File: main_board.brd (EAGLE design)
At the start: 100.3 x 74.9 mm, 46 parts, among them P1 ST-TF-003A, U1 STM32F407VGT6, U2 USBLC6-2, U3 MCP1700T-3302E, U4 LTC4054LES5-4.2#TRPBF, X1 MicroUSB-B

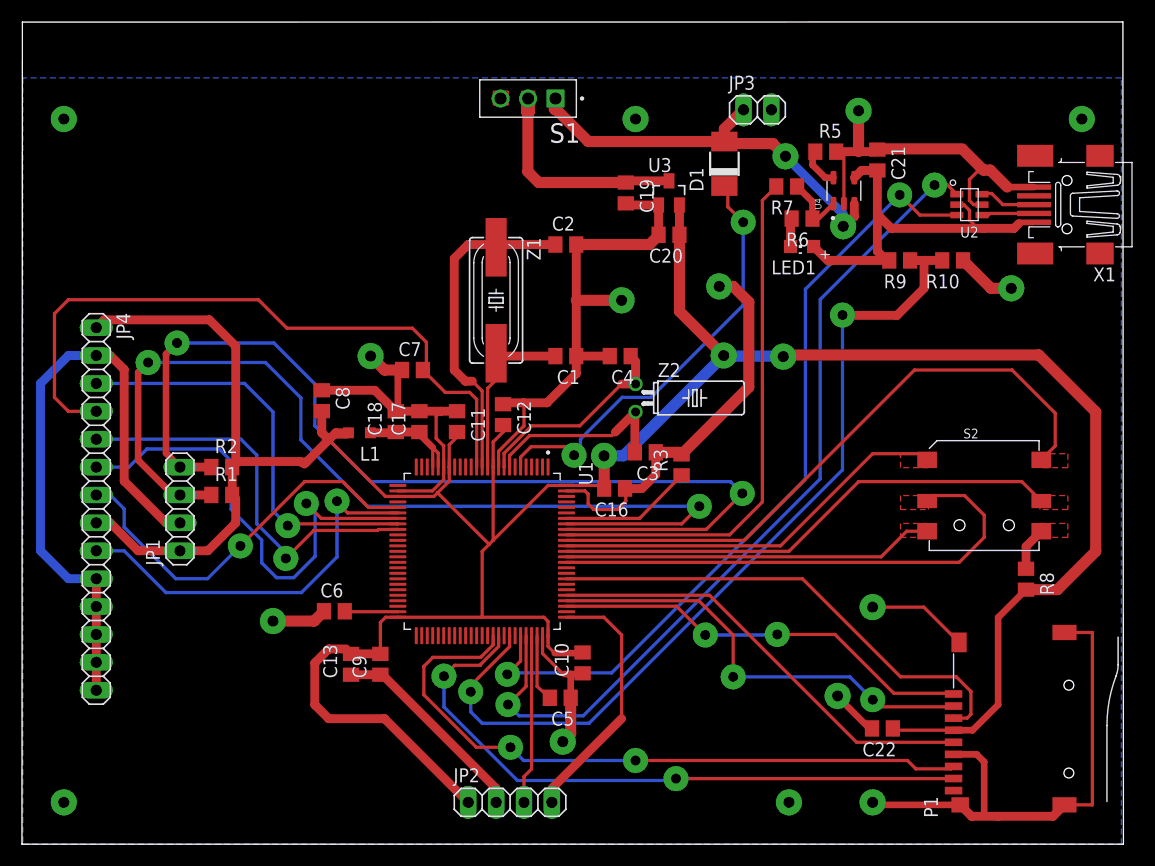
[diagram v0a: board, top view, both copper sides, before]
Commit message: correct board errors
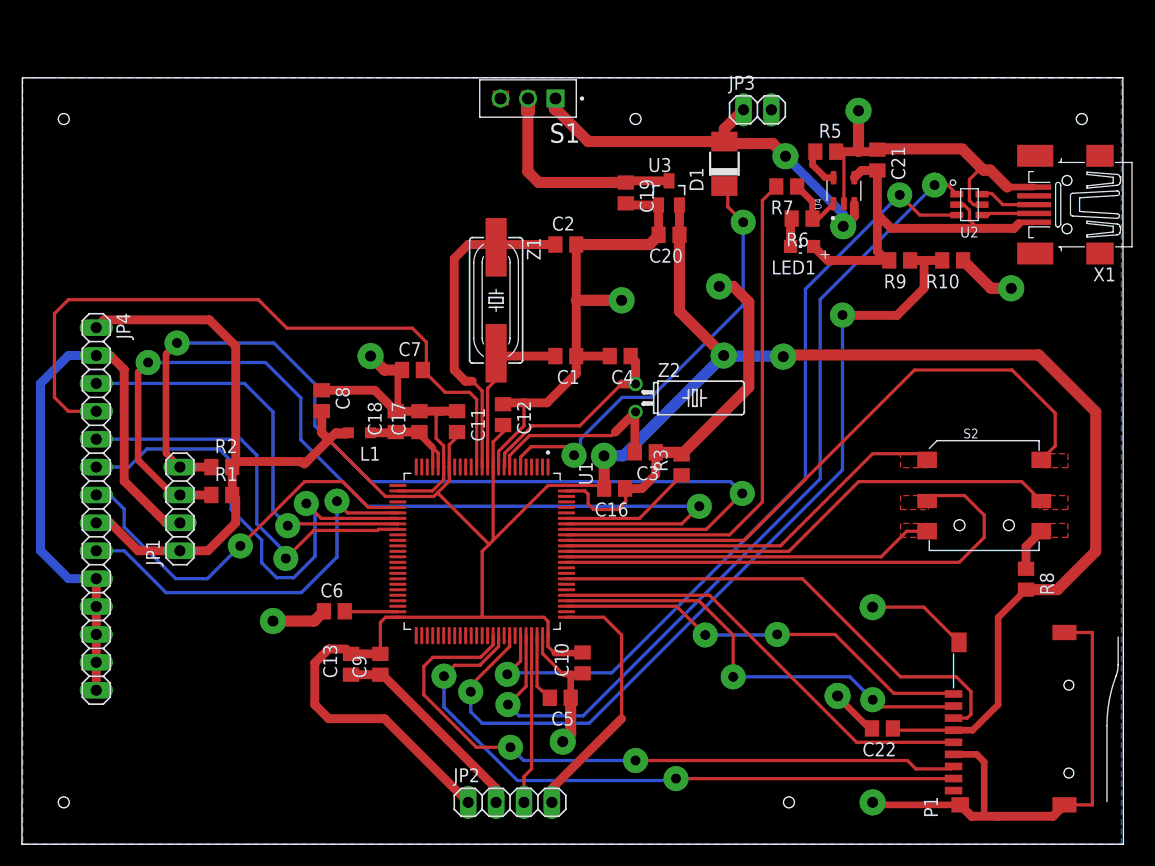
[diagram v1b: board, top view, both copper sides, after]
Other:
- board size 100.3 x 74.9 mm -> 100.3 x 69.8 mm
